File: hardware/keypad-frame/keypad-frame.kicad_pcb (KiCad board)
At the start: 2 copper layers, 150.2 x 64.2 mm, 13 parts, among them SW2 Switch_SW_Push, SW3 Switch_SW_Push, SW4 Switch_SW_Push, SW5 Switch_SW_Push, SW6 Switch_SW_Push, SW7 Switch_SW_Push, U3 IE096HQ1301CL_SLOT, U4 IE096HQ1301CL_SLOT, U5 IE096HQ1301CL_SLOT, U6 IE096HQ1301CL_SLOT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

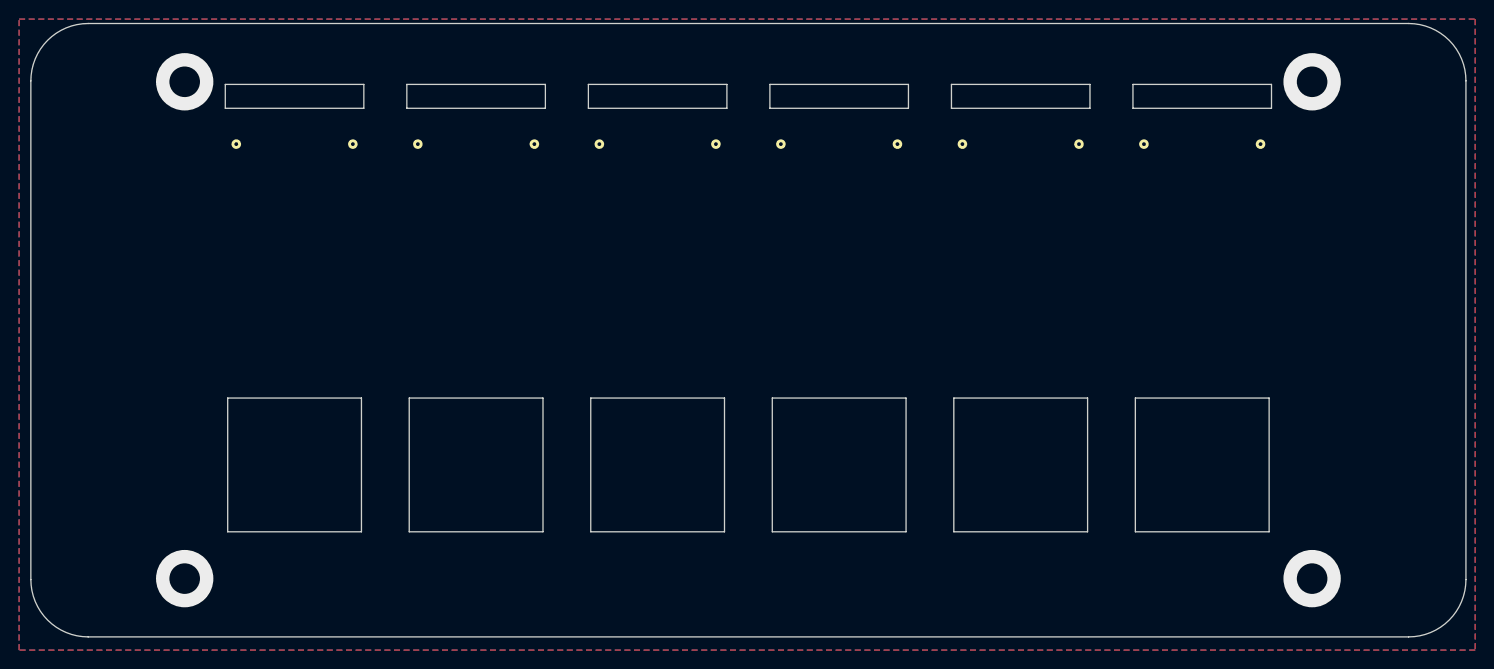
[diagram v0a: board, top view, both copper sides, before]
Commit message: hardware/keypad-frame: Sep2022a version
Reduced keyswitch opening by 0.2mm
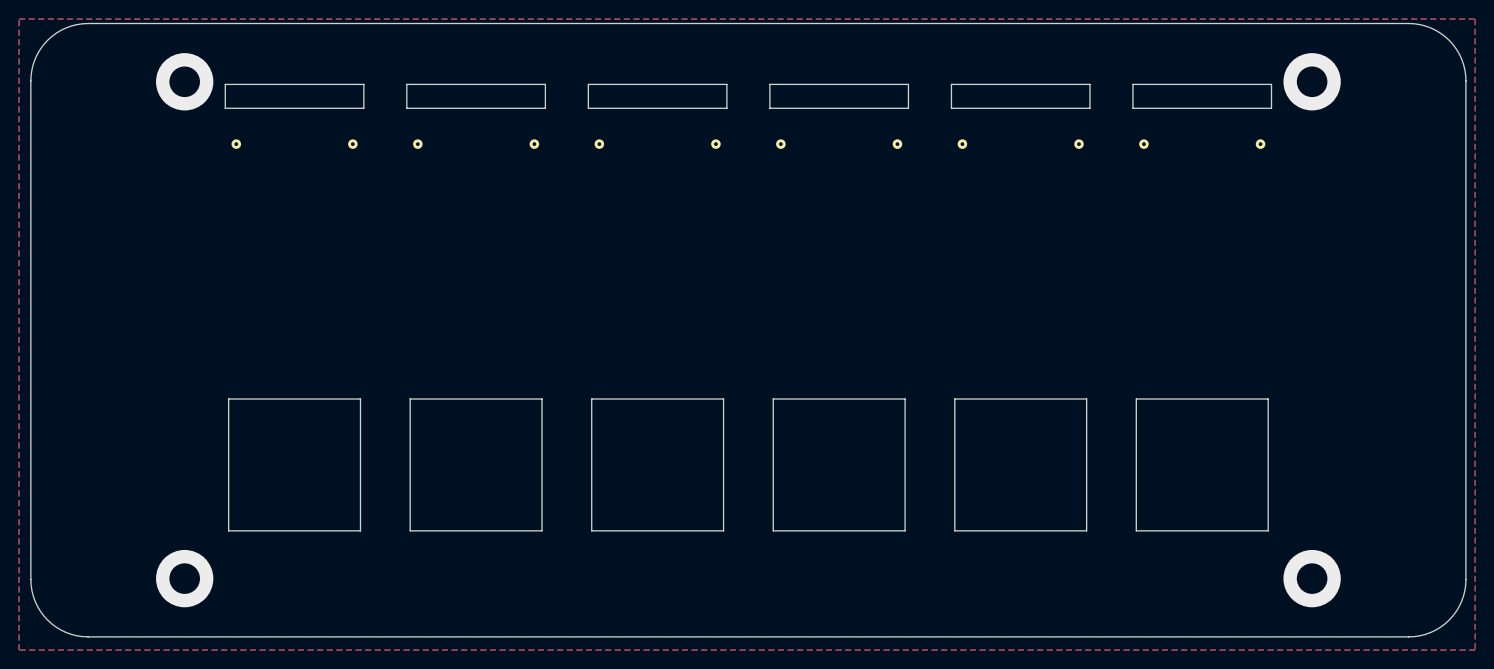
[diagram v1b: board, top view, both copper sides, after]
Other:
- net class Default removed
- board text added: "keypad-frame @TomKeddie Sep2022"
- board text removed: "keypad-frame @TomKeddie May2021"
